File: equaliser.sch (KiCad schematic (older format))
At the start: 33 parts, among them U12 NE5532

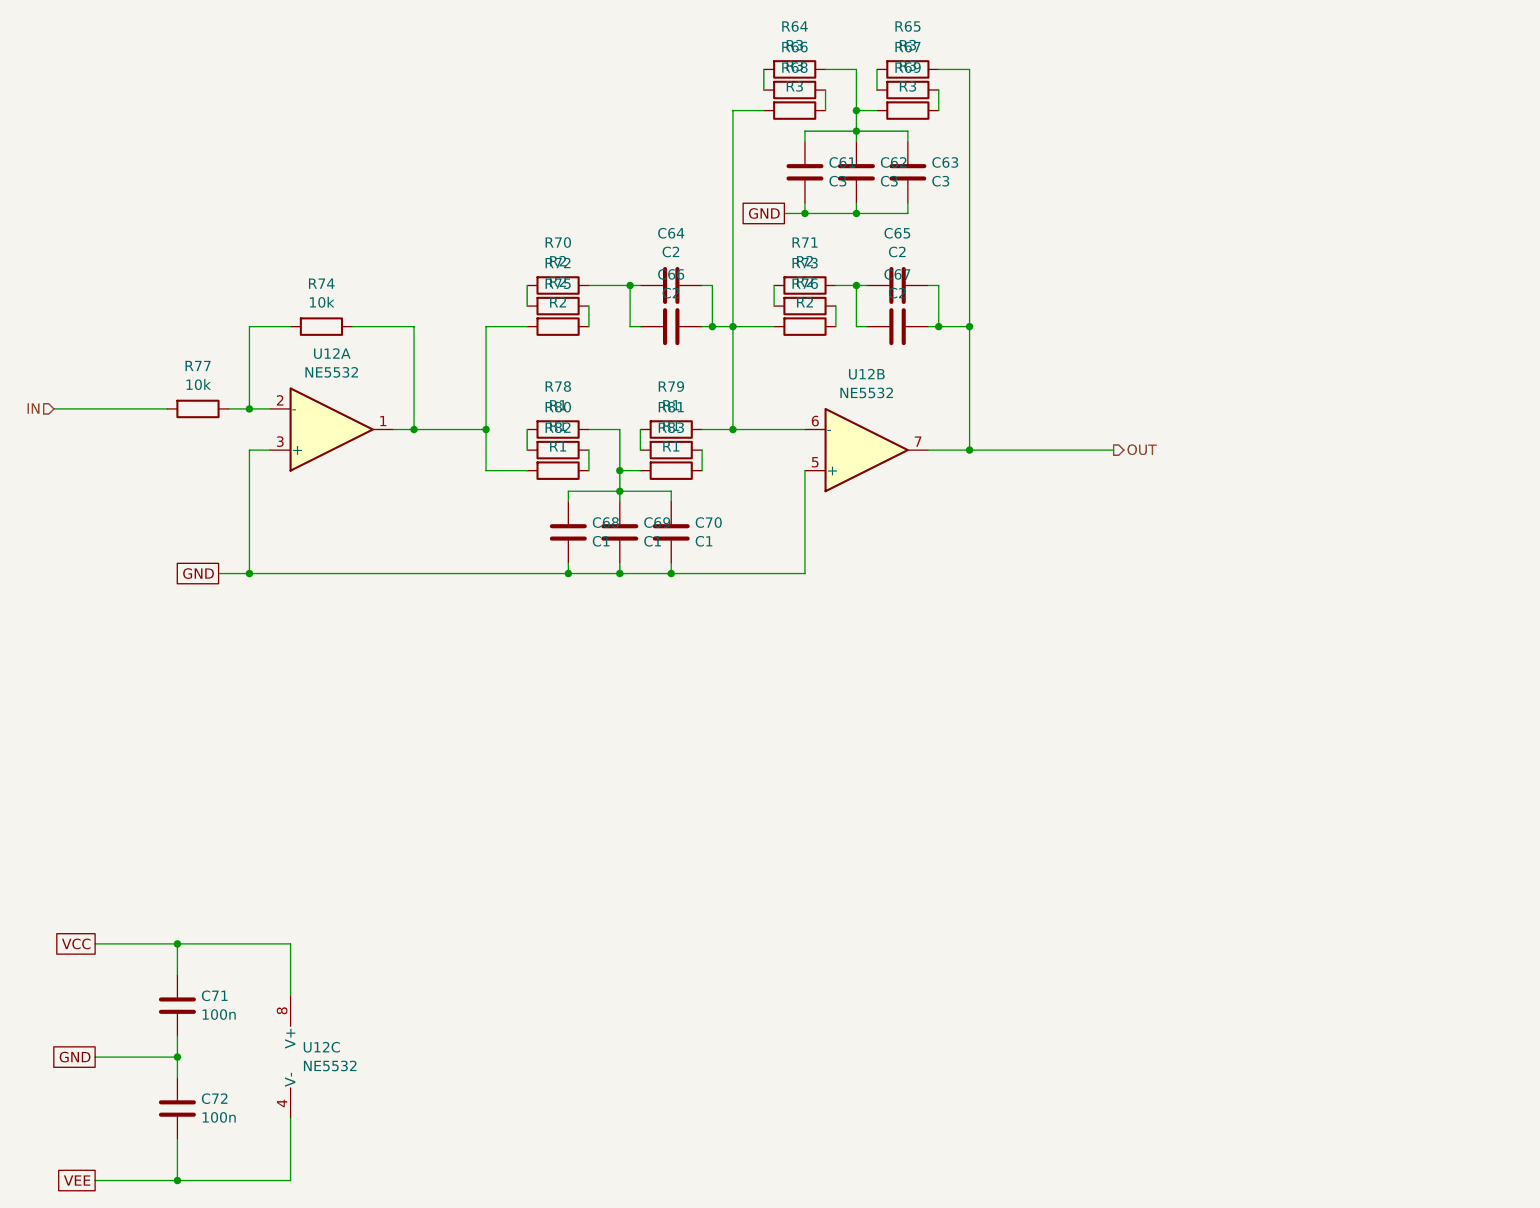
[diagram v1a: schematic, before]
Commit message: added buffered volume pot, and fixed subsonic filter added signal taps for external transforms/filters to be added later
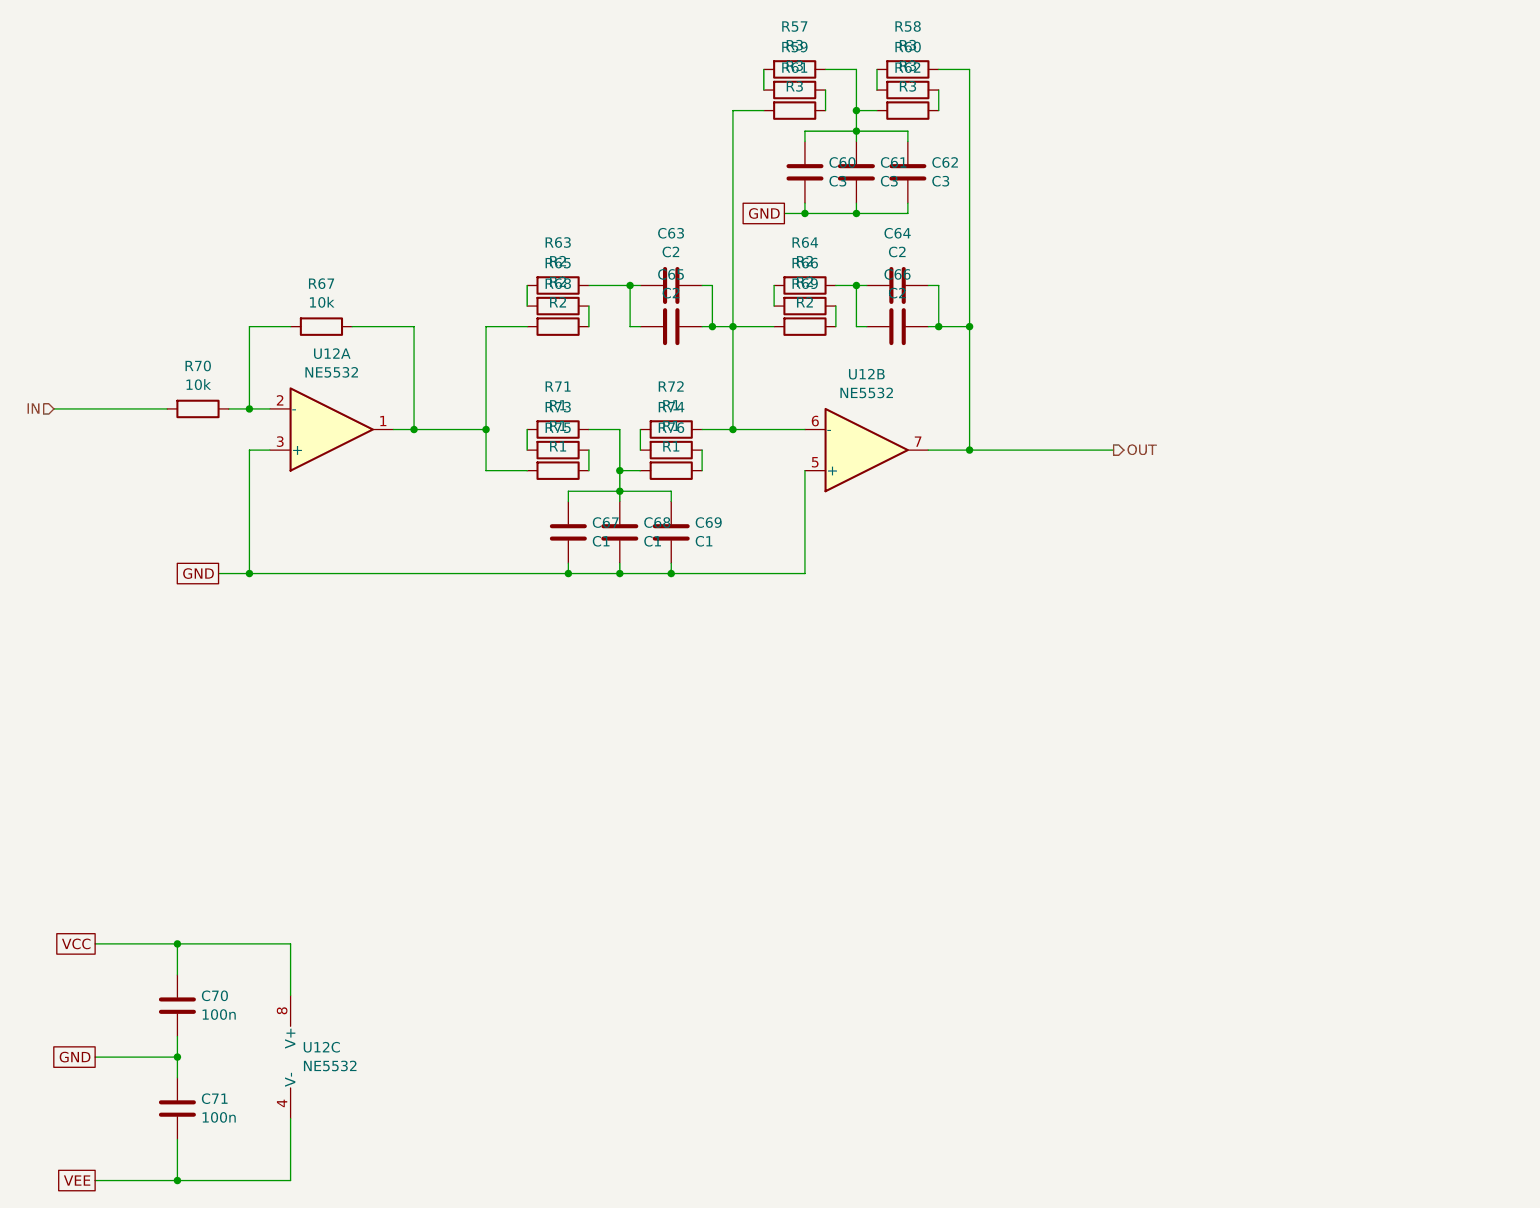
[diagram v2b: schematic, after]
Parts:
- renumbered C61 to C60, C62 to C61, C63 to C62, C64 to C63, C65 to C64, C66 to C65, C67 to C66, C68 to C67, C69 to C68, C70 to C69, C71 to C70, C72 to C71, R64 to R57, R65 to R58, R66 to R59, R67 to R60, R68 to R61, R69 to R62, R70 to R63, R71 to R64, R72 to R65, R73 to R66, R74 to R67, R75 to R68, R76 to R69, R77 to R70, R78 to R71, R79 to R72, R80 to R73, R81 to R74, R82 to R75, R83 to R76
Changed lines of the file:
@@
 $Descr A4 11693 8268
 encoding utf-8
-Sheet 12 13
+Sheet 11 19
 Title "Linkwitz Transform"
 Date "2021-10-03"
@@
 AR Path="/61597705/618769B5" Ref="C?"  Part="1"
 AR Path="/615C4B58/618769B5" Ref="C?"  Part="1"
-AR Path="/616914EE/618769B5" Ref="C72"  Part="1"
-F 0 "C72" H 1865 7046 50  0000 L CNN
+AR Path="/616914EE/618769B5" Ref="C71"  Part="1"
+F 0 "C71" H 1865 7046 50  0000 L CNN
 F 1 "100n" H 1865 6955 50  0000 L CNN
 F 2 "Capacitors_SMD:C_0805" H 1788 6850 50  0001 C CNN
@@
 AR Path="/61597705/618769BB" Ref="C?"  Part="1"
 AR Path="/615C4B58/618769BB" Ref="C?"  Part="1"
-AR Path="/616914EE/618769BB" Ref="C71"  Part="1"
-F 0 "C71" H 1865 6546 50  0000 L CNN
+AR Path="/616914EE/618769BB" Ref="C70"  Part="1"
+F 0 "C70" H 1865 6546 50  0000 L CNN
 F 1 "100n" H 1865 6455 50  0000 L CNN
 F 2 "Capacitors_SMD:C_0805" H 1788 6350 50  0001 C CNN
@@
 $EndComp
 $Comp
-L Device:R R74
+L Device:R R67
 U 1 1 6187BC3E
 P 2450 3200
-F 0 "R74" V 2243 3200 50  0000 C CNN
+F 0 "R67" V 2243 3200 50  0000 C CNN
 F 1 "10k" V 2334 3200 50  0000 C CNN
 F 2 "Resistors_SMD:R_0805" V 2380 3200 50  0001 C CNN
@@
 $EndComp
 $Comp
-L Device:R R77
+L Device:R R70
 U 1 1 6187C5F0
 P 1850 3600
-F 0 "R77" V 1643 3600 50  0000 C CNN
+F 0 "R70" V 1643 3600 50  0000 C CNN
 F 1 "10k" V 1734 3600 50  0000 C CNN
 F 2 "Resistors_SMD:R_0805" V 1780 3600 50  0001 C CNN
@@
 GND
 $Comp
-L Device:R R75
+L Device:R R68
 U 1 1 61887A13
 P 3600 3200
-F 0 "R75" V 3393 3200 50  0000 C CNN
+F 0 "R68" V 3393 3200 50  0000 C CNN
 F 1 "R2" V 3484 3200 50  0000 C CNN
 F 2 "Resistors_SMD:R_0805" V 3530 3200 50  0001 C CNN
@@
 $EndComp
 $Comp
-L Device:R R72
+L Device:R R65
 U 1 1 618881D6
 P 3600 3100
-F 0 "R72" V 3393 3100 50  0000 C CNN
+F 0 "R65" V 3393 3100 50  0000 C CNN
 F 1 "R2" V 3484 3100 50  0000 C CNN
 F 2 "Resistors_SMD:R_0805" V 3530 3100 50  0001 C CNN
@@
 $EndComp
 $Comp
-L Device:R R70
+L Device:R R63
 U 1 1 6188AB3F
 P 3600 3000
-F 0 "R70" V 3393 3000 50  0000 C CNN
+F 0 "R63" V 3393 3000 50  0000 C CNN
 F 1 "R2" V 3484 3000 50  0000 C CNN
 F 2 "Resistors_SMD:R_0805" V 3530 3000 50  0001 C CNN
@@
 $EndComp
 $Comp
-L Device:C C66
+L Device:C C65
 U 1 1 6188B0E8
 P 4150 3200
-F 0 "C66" V 3898 3200 50  0000 C CNN
+F 0 "C65" V 3898 3200 50  0000 C CNN
 F 1 "C2" V 3989 3200 50  0000 C CNN
 F 2 "Capacitors_ThroughHole:C_Rect_L10.0mm_W5.0mm_P5.00mm_P7.50mm" H 4188 3050 50  0001 C CNN
@@
 	3450 3100 3450 3000
 $Comp
-L Device:R R76
+L Device:R R69
 U 1 1 6188EADB
 P 4800 3200
-F 0 "R76" V 4593 3200 50  0000 C CNN
+F 0 "R69" V 4593 3200 50  0000 C CNN
 F 1 "R2" V 4684 3200 50  0000 C CNN
 F 2 "Resistors_SMD:R_0805" V 4730 3200 50  0001 C CNN
@@
 $EndComp
 $Comp
-L Device:R R73
+L Device:R R66
 U 1 1 6188EAE1
 P 4800 3100
-F 0 "R73" V 4593 3100 50  0000 C CNN
+F 0 "R66" V 4593 3100 50  0000 C CNN
 F 1 "R2" V 4684 3100 50  0000 C CNN
 F 2 "Resistors_SMD:R_0805" V 4730 3100 50  0001 C CNN
@@
 $EndComp
 $Comp
-L Device:R R71
+L Device:R R64
 U 1 1 6188EAE7
 P 4800 3000
-F 0 "R71" V 4593 3000 50  0000 C CNN
+F 0 "R64" V 4593 3000 50  0000 C CNN
 F 1 "R2" V 4684 3000 50  0000 C CNN
 F 2 "Resistors_SMD:R_0805" V 4730 3000 50  0001 C CNN
@@
 $EndComp
 $Comp
-L Device:C C67
+L Device:C C66
 U 1 1 6188EAED
 P 5250 3200
-F 0 "C67" V 4998 3200 50  0000 C CNN
+F 0 "C66" V 4998 3200 50  0000 C CNN
 F 1 "C2" V 5089 3200 50  0000 C CNN
 F 2 "Capacitors_ThroughHole:C_Rect_L10.0mm_W5.0mm_P5.00mm_P7.50mm" H 5288 3050 50  0001 C CNN
@@
 	4950 3000 5050 3000
 $Comp
-L Device:R R82
+L Device:R R75
 U 1 1 61891898
 P 3600 3900
-F 0 "R82" V 3393 3900 50  0000 C CNN
+F 0 "R75" V 3393 3900 50  0000 C CNN
 F 1 "R1" V 3484 3900 50  0000 C CNN
 F 2 "Resistors_SMD:R_0805" V 3530 3900 50  0001 C CNN
@@
 $EndComp
 $Comp
-L Device:R R80
+L Device:R R73
 U 1 1 6189189E
 P 3600 3800
-F 0 "R80" V 3393 3800 50  0000 C CNN
+F 0 "R73" V 3393 3800 50  0000 C CNN
 F 1 "R1" V 3484 3800 50  0000 C CNN
 F 2 "Resistors_SMD:R_0805" V 3530 3800 50  0001 C CNN
@@
 $EndComp
 $Comp
-L Device:R R78
+L Device:R R71
 U 1 1 618918A4
 P 3600 3700
-F 0 "R78" V 3393 3700 50  0000 C CNN
+F 0 "R71" V 3393 3700 50  0000 C CNN
 F 1 "R1" V 3484 3700 50  0000 C CNN
 F 2 "Resistors_SMD:R_0805" V 3530 3700 50  0001 C CNN
@@
 	3450 3800 3450 3700
 $Comp
-L Device:R R83
+L Device:R R76
 U 1 1 61893819
 P 4150 3900
-F 0 "R83" V 3943 3900 50  0000 C CNN
+F 0 "R76" V 3943 3900 50  0000 C CNN
 F 1 "R1" V 4034 3900 50  0000 C CNN
 F 2 "Resistors_SMD:R_0805" V 4080 3900 50  0001 C CNN
@@
 $EndComp
 $Comp
-L Device:R R81
+L Device:R R74
 U 1 1 6189381F
 P 4150 3800
-F 0 "R81" V 3943 3800 50  0000 C CNN
+F 0 "R74" V 3943 3800 50  0000 C CNN
 F 1 "R1" V 4034 3800 50  0000 C CNN
 F 2 "Resistors_SMD:R_0805" V 4080 3800 50  0001 C CNN
@@
 $EndComp
 $Comp
-L Device:R R79
+L Device:R R72
 U 1 1 61893825
 P 4150 3700
-F 0 "R79" V 3943 3700 50  0000 C CNN
+F 0 "R72" V 3943 3700 50  0000 C CNN
 F 1 "R1" V 4034 3700 50  0000 C CNN
 F 2 "Resistors_SMD:R_0805" V 4080 3700 50  0001 C CNN
@@
 	4300 3200 4350 3200
 $Comp
-L Device:C C68
+L Device:C C67
 U 1 1 6189B712
 P 3650 4200
-F 0 "C68" H 3765 4246 50  0000 L CNN
+F 0 "C67" H 3765 4246 50  0000 L CNN
 F 1 "C1" H 3765 4155 50  0000 L CNN
 F 2 "Capacitors_ThroughHole:C_Rect_L10.0mm_W5.0mm_P5.00mm_P7.50mm" H 3688 4050 50  0001 C CNN
@@
 	5600 3800 5400 3800
 $Comp
-L Device:R R68
+L Device:R R61
 U 1 1 618B4E04
 P 4750 2150
-F 0 "R68" V 4543 2150 50  0000 C CNN
+F 0 "R61" V 4543 2150 50  0000 C CNN
 F 1 "R3" V 4634 2150 50  0000 C CNN
 F 2 "Resistors_SMD:R_0805" V 4680 2150 50  0001 C CNN
@@
 $EndComp
 $Comp
-L Device:R R66
+L Device:R R59
 U 1 1 618B4E0A
 P 4750 2050
-F 0 "R66" V 4543 2050 50  0000 C CNN
+F 0 "R59" V 4543 2050 50  0000 C CNN
 F 1 "R3" V 4634 2050 50  0000 C CNN
 F 2 "Resistors_SMD:R_0805" V 4680 2050 50  0001 C CNN
@@
 $EndComp
 $Comp
-L Device:R R64
+L Device:R R57
 U 1 1 618B4E10
 P 4750 1950
-F 0 "R64" V 4543 1950 50  0000 C CNN
+F 0 "R57" V 4543 1950 50  0000 C CNN
 F 1 "R3" V 4634 1950 50  0000 C CNN
 F 2 "Resistors_SMD:R_0805" V 4680 1950 50  0001 C CNN
@@
 	4600 2050 4600 1950
 $Comp
-L Device:R R69
+L Device:R R62
 U 1 1 618B4E18
 P 5300 2150
-F 0 "R69" V 5093 2150 50  0000 C CNN
+F 0 "R62" V 5093 2150 50  0000 C CNN
 F 1 "R3" V 5184 2150 50  0000 C CNN
 F 2 "Resistors_SMD:R_0805" V 5230 2150 50  0001 C CNN
@@
 $EndComp
 $Comp
-L Device:R R67
+L Device:R R60
 U 1 1 618B4E1E
 P 5300 2050
-F 0 "R67" V 5093 2050 50  0000 C CNN
+F 0 "R60" V 5093 2050 50  0000 C CNN
 F 1 "R3" V 5184 2050 50  0000 C CNN
 F 2 "Resistors_SMD:R_0805" V 5230 2050 50  0001 C CNN
@@
 $EndComp
 $Comp
-L Device:R R65
+L Device:R R58
 U 1 1 618B4E24
 P 5300 1950
-F 0 "R65" V 5093 1950 50  0000 C CNN
+F 0 "R58" V 5093 1950 50  0000 C CNN
 F 1 "R3" V 5184 1950 50  0000 C CNN
 F 2 "Resistors_SMD:R_0805" V 5230 1950 50  0001 C CNN
@@
 Connection ~ 5050 2150
 $Comp
-L Device:C C61
+L Device:C C60
 U 1 1 618B4E39
 P 4800 2450
-F 0 "C61" H 4915 2496 50  0000 L CNN
+F 0 "C60" H 4915 2496 50  0000 L CNN
 F 1 "C3" H 4915 2405 50  0000 L CNN
 F 2 "Capacitors_ThroughHole:C_Rect_L10.0mm_W5.0mm_P5.00mm_P7.50mm" H 4838 2300 50  0001 C CNN
@@
 	5400 3200 5450 3200
 $Comp
-L Device:C C64
+L Device:C C63
 U 1 1 6191FC2F
 P 4150 3000
-F 0 "C64" V 3898 3000 50  0000 C CNN
+F 0 "C63" V 3898 3000 50  0000 C CNN
 F 1 "C2" V 3989 3000 50  0000 C CNN
 F 2 "Capacitors_SMD:C_1210_HandSoldering" H 4188 2850 50  0001 C CNN
@@
 $EndComp
 $Comp
-L Device:C C65
+L Device:C C64
 U 1 1 61925A41
 P 5250 3000
-F 0 "C65" V 4998 3000 50  0000 C CNN
+F 0 "C64" V 4998 3000 50  0000 C CNN
 F 1 "C2" V 5089 3000 50  0000 C CNN
 F 2 "Capacitors_SMD:C_1210_HandSoldering" H 5288 2850 50  0001 C CNN
@@
 	5450 3200 5600 3200
 $Comp
-L Device:C C69
+L Device:C C68
 U 1 1 6193AE35
 P 3900 4200
-F 0 "C69" H 4015 4246 50  0000 L CNN
+F 0 "C68" H 4015 4246 50  0000 L CNN
 F 1 "C1" H 4015 4155 50  0000 L CNN
 F 2 "Capacitors_ThroughHole:C_Rect_L10.0mm_W5.0mm_P5.00mm_P7.50mm" H 3938 4050 50  0001 C CNN
@@
 $EndComp
 $Comp
-L Device:C C70
+L Device:C C69
 U 1 1 6193B2A1
 P 4150 4200
-F 0 "C70" H 4265 4246 50  0000 L CNN
+F 0 "C69" H 4265 4246 50  0000 L CNN
 F 1 "C1" H 4265 4155 50  0000 L CNN
 F 2 "Capacitors_ThroughHole:C_Rect_L10.0mm_W5.0mm_P5.00mm_P7.50mm" H 4188 4050 50  0001 C CNN
@@
 $EndComp
 $Comp
-L Device:C C62
+L Device:C C61
 U 1 1 6193C1FB
 P 5050 2450
-F 0 "C62" H 5165 2496 50  0000 L CNN
+F 0 "C61" H 5165 2496 50  0000 L CNN
 F 1 "C3" H 5165 2405 50  0000 L CNN
 F 2 "Capacitors_ThroughHole:C_Rect_L10.0mm_W5.0mm_P5.00mm_P7.50mm" H 5088 2300 50  0001 C CNN
@@
 $EndComp
 $Comp
-L Device:C C63
+L Device:C C62
 U 1 1 6193C690
 P 5300 2450
-F 0 "C63" H 5415 2496 50  0000 L CNN
+F 0 "C62" H 5415 2496 50  0000 L CNN
 F 1 "C3" H 5415 2405 50  0000 L CNN
 F 2 "Capacitors_ThroughHole:C_Rect_L10.0mm_W5.0mm_P5.00mm_P7.50mm" H 5338 2300 50  0001 C CNN

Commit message: inverted LF processing chain, now with BW2 subsonic filter
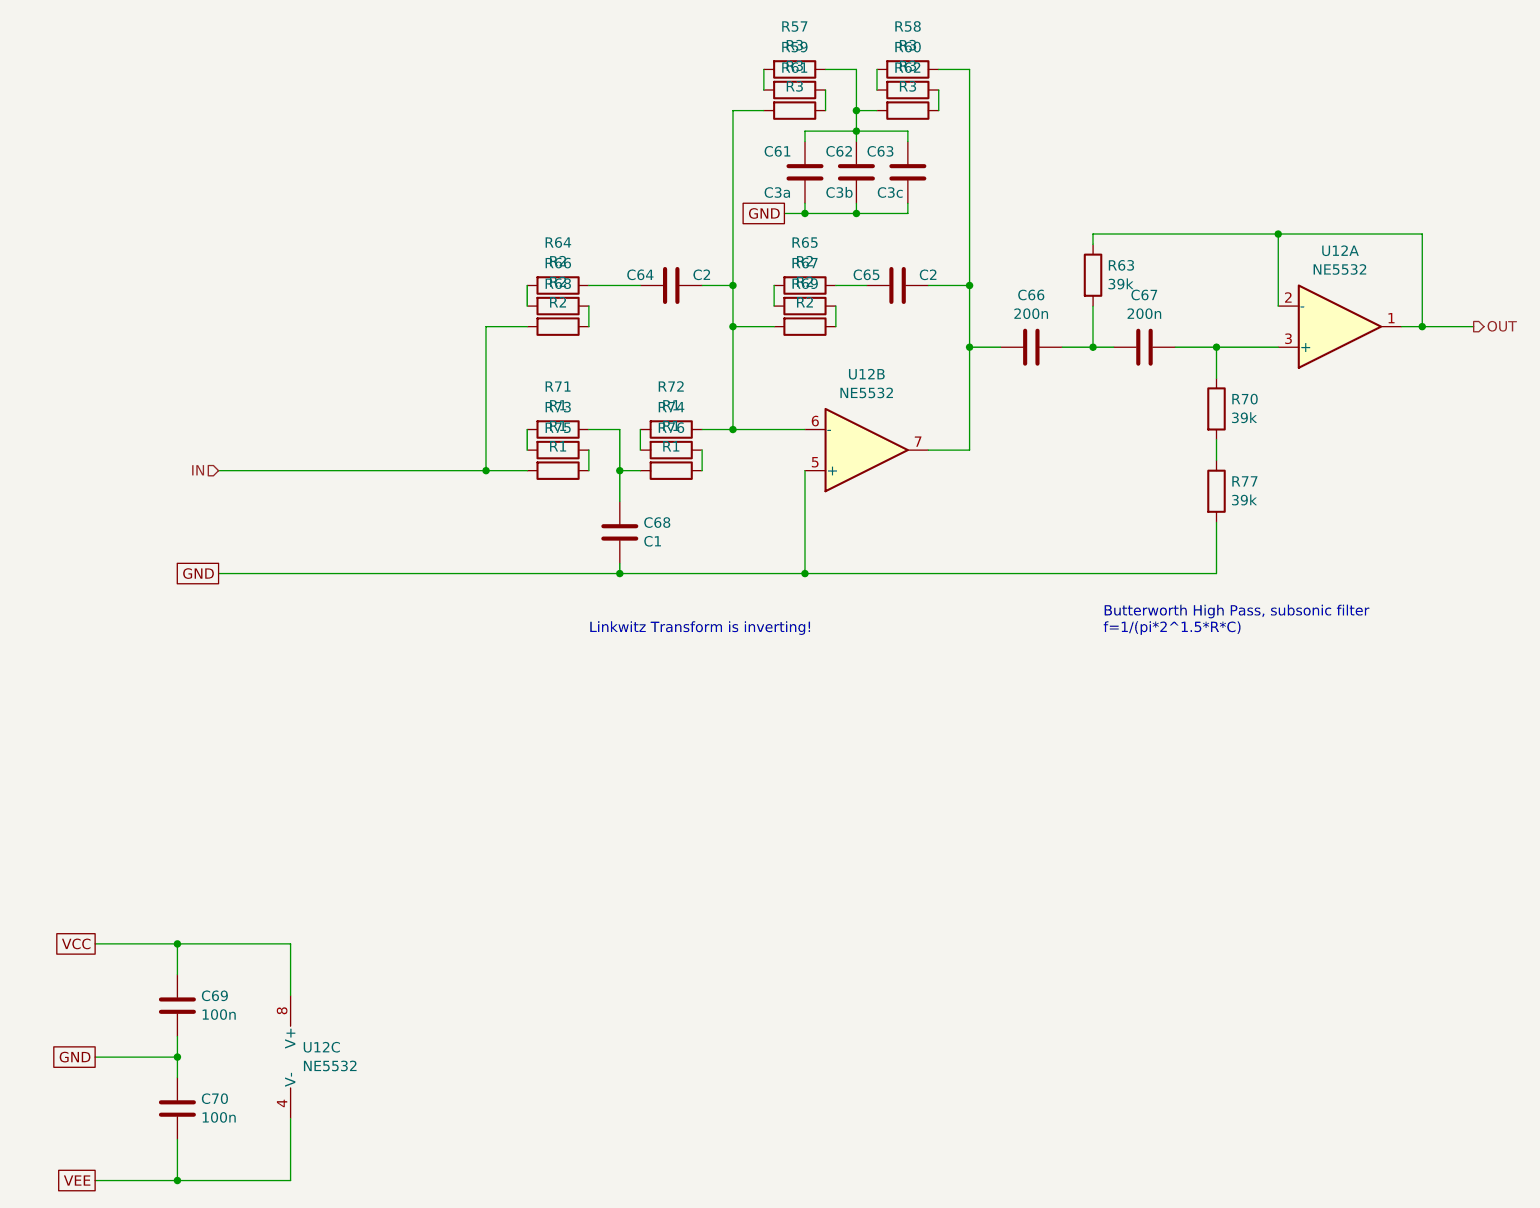
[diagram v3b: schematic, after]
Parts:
- removed C65: C2, Capacitors_ThroughHole:C_Rect_L10.0mm_W5.0mm_P5.00mm_P7.50mm, symbol Device:C
- removed C68, C69: C1, Capacitors_ThroughHole:C_Rect_L10.0mm_W5.0mm_P5.00mm_P7.50mm, symbol Device:C
- removed R67: 10k, Resistors_SMD:R_0805, symbol Device:R
- added C67: 200n, power:C_Rect_L7.0mm_W4.5mm_P5_1210x2_combo, symbol Device:C
- added R63, R77: 39k, Resistors_SMD:R_0805, symbol Device:R
- C61: renamed from C60; value C3 -> C3a; footprint Capacitors_ThroughHole:C_Rect_L10.0mm_W5.0mm_P5.00mm_P7.50mm -> power:C_Rect_L19.0mm_W11.0mm_combo
- C62: renamed from C61; value C3 -> C3b; footprint Capacitors_ThroughHole:C_Rect_L10.0mm_W5.0mm_P5.00mm_P7.50mm -> power:C_Rect_L7.0mm_W4.5mm_P5_1210_combo
- C63: renamed from C62; value C3 -> C3c; footprint Capacitors_ThroughHole:C_Rect_L10.0mm_W5.0mm_P5.00mm_P7.50mm -> power:C_Rect_L7.0mm_W4.5mm_P5_1210_combo
- C64: renamed from C63; footprint Capacitors_SMD:C_1210_HandSoldering -> power:C_Rect_L7.0mm_W4.5mm_P5_1210_combo
- C65: renamed from C64; footprint Capacitors_SMD:C_1210_HandSoldering -> power:C_Rect_L7.0mm_W4.5mm_P5_1210_combo
- C66: value C2 -> 200n; footprint Capacitors_ThroughHole:C_Rect_L10.0mm_W5.0mm_P5.00mm_P7.50mm -> power:C_Rect_L7.0mm_W4.5mm_P5_1210x2_combo
- C68: renamed from C67; footprint Capacitors_ThroughHole:C_Rect_L10.0mm_W5.0mm_P5.00mm_P7.50mm -> power:C_Rect_L19.0mm_W11.0mm_combo
- R70: value 10k -> 39k
- U12: footprint (none) -> Housings_DIP:DIP-8_W7.62mm_Socket
- renumbered C70 to C69, C71 to C70, R63 to R64, R64 to R65, R65 to R66, R66 to R67
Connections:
- net GND: now also R77.2; no longer U12.3 (+)
- net IN: now also R68.2, R75.2; no longer R70.2
- net OUT: now also U12.1, U12.2 (-), R63.1; no longer C65.1, C66.1, R58.1, U12.7
- net at R70.1: now also U12.3 (+), C67.1; no longer U12.2 (-)
- net at C65.2, R65.1: no longer C66.2
- new net: C65.1, C66.2, R58.1, U12.7
- new net: R70.2, R77.1
- new net: C66.1, C67.2, R63.2
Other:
- note added: "Butterworth High Pass, subsonic filter\nf=1/(pi*2^1.5*R*C)"
- note added: "Linkwitz Transform is inverting!"
- moved on the sheet: C68
